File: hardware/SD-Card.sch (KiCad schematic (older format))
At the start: 14 parts

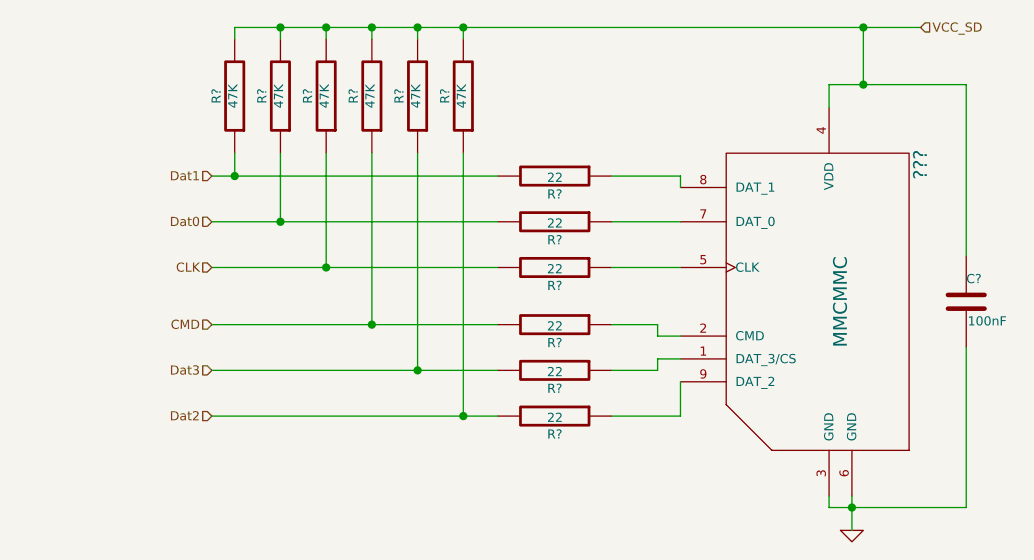
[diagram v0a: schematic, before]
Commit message: Arreglada la distribucion de pines
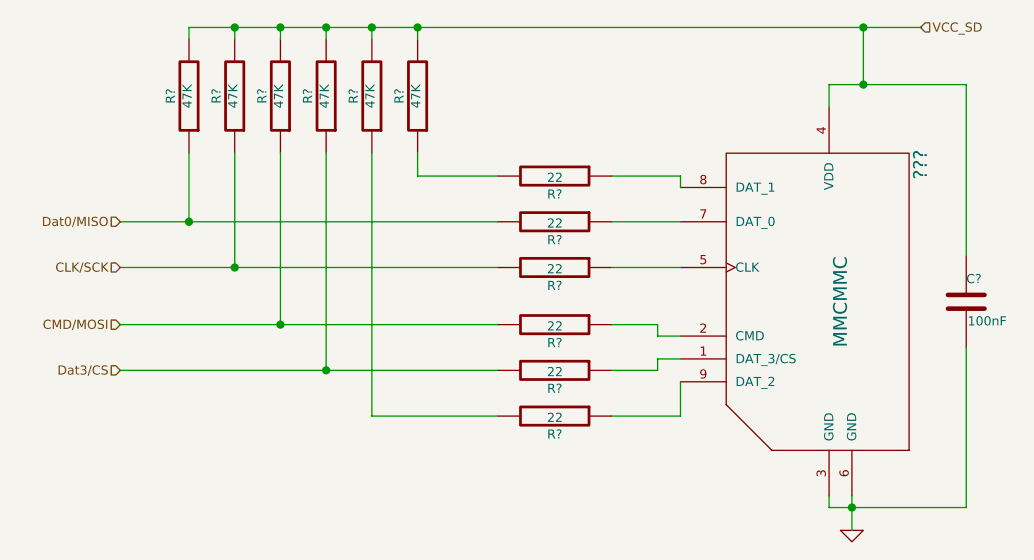
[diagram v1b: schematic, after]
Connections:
- net CLK renamed CLK/SCK
- net CMD renamed CMD/MOSI
- net Dat0 renamed Dat0/MISO
- net Dat1: no longer names the net of R?.1, R?.2
- net Dat2: no longer names the net of R?.1, R?.2
- net Dat3 renamed Dat3/CS
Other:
- moved on the sheet: R?
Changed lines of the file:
@@
 L R R?
 U 1 1 53E03706
-P 4100 2700
-F 0 "R?" V 4180 2700 40  0000 C CNN
-F 1 "47K" V 4107 2701 40  0000 C CNN
-F 2 "" V 4030 2700 30  0000 C CNN
-F 3 "" H 4100 2700 30  0000 C CNN
-	1    4100 2700
+P 3700 2700
+F 0 "R?" V 3780 2700 40  0000 C CNN
+F 1 "47K" V 3707 2701 40  0000 C CNN
+F 2 "" V 3630 2700 30  0000 C CNN
+F 3 "" H 3700 2700 30  0000 C CNN
+	1    3700 2700
 	-1   0    0    1
 $EndComp
@@
 L R R?
 U 1 1 53E03953
+P 3500 2700
+F 0 "R?" V 3580 2700 40  0000 C CNN
+F 1 "47K" V 3507 2701 40  0000 C CNN
+F 2 "" V 3430 2700 30  0000 C CNN
+F 3 "" H 3500 2700 30  0000 C CNN
+	1    3500 2700
+	-1   0    0    1
+$EndComp
+$Comp
+L R R?
+U 1 1 53E0395E
+P 3300 2700
+F 0 "R?" V 3380 2700 40  0000 C CNN
+F 1 "47K" V 3307 2701 40  0000 C CNN
+F 2 "" V 3230 2700 30  0000 C CNN
+F 3 "" H 3300 2700 30  0000 C CNN
+	1    3300 2700
+	-1   0    0    1
+$EndComp
+$Comp
+L R R?
+U 1 1 53E03969
+P 3100 2700
+F 0 "R?" V 3180 2700 40  0000 C CNN
+F 1 "47K" V 3107 2701 40  0000 C CNN
+F 2 "" V 3030 2700 30  0000 C CNN
+F 3 "" H 3100 2700 30  0000 C CNN
+	1    3100 2700
+	-1   0    0    1
+$EndComp
+$Comp
+L R R?
+U 1 1 53E03974
+P 2900 2700
+F 0 "R?" V 2980 2700 40  0000 C CNN
+F 1 "47K" V 2907 2701 40  0000 C CNN
+F 2 "" V 2830 2700 30  0000 C CNN
+F 3 "" H 2900 2700 30  0000 C CNN
+	1    2900 2700
+	-1   0    0    1
+$EndComp
+$Comp
+L R R?
+U 1 1 53E0397F
 P 3900 2700
 F 0 "R?" V 3980 2700 40  0000 C CNN
@@
 	-1   0    0    1
 $EndComp
-$Comp
-L R R?
-U 1 1 53E0395E
-P 3700 2700
-F 0 "R?" V 3780 2700 40  0000 C CNN
-F 1 "47K" V 3707 2701 40  0000 C CNN
-F 2 "" V 3630 2700 30  0000 C CNN
-F 3 "" H 3700 2700 30  0000 C CNN
-	1    3700 2700
-	-1   0    0    1
-$EndComp
-$Comp
-L R R?
-U 1 1 53E03969
-P 3500 2700
-F 0 "R?" V 3580 2700 40  0000 C CNN
-F 1 "47K" V 3507 2701 40  0000 C CNN
-F 2 "" V 3430 2700 30  0000 C CNN
-F 3 "" H 3500 2700 30  0000 C CNN
-	1    3500 2700
-	-1   0    0    1
-$EndComp
-$Comp
-L R R?
-U 1 1 53E03974
-P 3300 2700
-F 0 "R?" V 3380 2700 40  0000 C CNN
-F 1 "47K" V 3307 2701 40  0000 C CNN
-F 2 "" V 3230 2700 30  0000 C CNN
-F 3 "" H 3300 2700 30  0000 C CNN
-	1    3300 2700
-	-1   0    0    1
-$EndComp
-$Comp
-L R R?
-U 1 1 53E0397F
-P 3100 2700
-F 0 "R?" V 3180 2700 40  0000 C CNN
-F 1 "47K" V 3107 2701 40  0000 C CNN
-F 2 "" V 3030 2700 30  0000 C CNN
-F 3 "" H 3100 2700 30  0000 C CNN
-	1    3100 2700
-	-1   0    0    1
-$EndComp
-Text HLabel 3000 3050 0    40   Input ~ 0
-Dat1
-Text HLabel 3000 3250 0    40   Input ~ 0
-Dat0
-Text HLabel 3000 3450 0    40   Input ~ 0
-CLK
-Text HLabel 3000 3700 0    40   Input ~ 0
-CMD
-Text HLabel 3000 3900 0    40   Input ~ 0
-Dat3
-Text HLabel 3000 4100 0    40   Input ~ 0
-Dat2
+Text HLabel 2600 3250 0    40   Input ~ 0
+Dat0/MISO
+Text HLabel 2600 3450 0    40   Input ~ 0
+CLK/SCK
+Text HLabel 2600 3700 0    40   Input ~ 0
+CMD/MOSI
+Text HLabel 2600 3900 0    40   Input ~ 0
+Dat3/CS
 Text HLabel 6100 2400 2    40   Input ~ 0
 VCC_SD
 Wire Wire Line
-	3000 3050 4250 3050
-Wire Wire Line
-	3000 3250 4250 3250
-Wire Wire Line
-	3000 3450 4250 3450
-Wire Wire Line
-	3000 3700 4250 3700
-Wire Wire Line
-	3000 3900 4250 3900
-Wire Wire Line
-	3000 4100 4250 4100
-Wire Wire Line
-	4100 2950 4100 4100
-Connection ~ 4100 4100
-Wire Wire Line
-	3900 2950 3900 3900
-Connection ~ 3900 3900
-Wire Wire Line
-	3700 2950 3700 3700
-Connection ~ 3700 3700
-Wire Wire Line
-	3500 2950 3500 3450
-Connection ~ 3500 3450
-Wire Wire Line
-	3300 2950 3300 3250
-Connection ~ 3300 3250
-Wire Wire Line
-	3100 2950 3100 3050
-Connection ~ 3100 3050
+	2600 3250 4250 3250
+Wire Wire Line
+	2600 3450 4250 3450
+Wire Wire Line
+	2600 3700 4250 3700
+Wire Wire Line
+	2600 3900 4250 3900
+Wire Wire Line
+	3700 2950 3700 4100
+Wire Wire Line
+	3500 2950 3500 3900
+Connection ~ 3500 3900
+Wire Wire Line
+	3300 2950 3300 3700
+Connection ~ 3300 3700
+Wire Wire Line
+	3100 2950 3100 3450
+Connection ~ 3100 3450
+Wire Wire Line
+	2900 2950 2900 3250
+Connection ~ 2900 3250
+Wire Wire Line
+	3900 2950 3900 3050
 $Comp
 L C C?
@@
 Connection ~ 5800 4500
 Wire Wire Line
-	3100 2400 6100 2400
-Wire Wire Line
 	5850 2400 5850 2650
 Connection ~ 5850 2650
 Wire Wire Line
+	3700 2400 3700 2450
+Wire Wire Line
+	3500 2450 3500 2400
+Connection ~ 3500 2400
+Wire Wire Line
+	3300 2450 3300 2400
+Connection ~ 3300 2400
+Wire Wire Line
 	3100 2450 3100 2400
-Wire Wire Line
-	4100 2400 4100 2450
+Connection ~ 3100 2400
+Wire Wire Line
+	2900 2450 2900 2400
+Connection ~ 3700 2400
+Connection ~ 5850 2400
+Wire Wire Line
+	3900 3050 4250 3050
 Wire Wire Line
 	3900 2450 3900 2400
 Connection ~ 3900 2400
 Wire Wire Line
-	3700 2450 3700 2400
-Connection ~ 3700 2400
-Wire Wire Line
-	3500 2450 3500 2400
-Connection ~ 3500 2400
-Wire Wire Line
-	3300 2450 3300 2400
-Connection ~ 3300 2400
-Connection ~ 4100 2400
-Connection ~ 5850 2400
+	3700 4100 4250 4100
+Wire Wire Line
+	2900 2400 6100 2400
 $EndSCHEMATC

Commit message: Terminado el esquematico, iniciado el PCB
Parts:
- C17: renamed from C?; footprint (none) -> Capacitors_SMD:c_1206
- R50, R51, R52, R53, R54, R55, R56, R57, R58, R59, R60, R61: renamed from R?; footprint (none) -> Resistors_SMD:Resistor_SMD1206_ReflowWave
- S1: renamed from ???; value MMCMMC -> SD
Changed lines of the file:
@@
 $EndDescr
 $Comp
-L R R?
+L R R54
 U 1 1 53E03706
 P 3700 2700
-F 0 "R?" V 3780 2700 40  0000 C CNN
+F 0 "R54" V 3780 2700 40  0000 C CNN
 F 1 "47K" V 3707 2701 40  0000 C CNN
-F 2 "" V 3630 2700 30  0000 C CNN
+F 2 "Resistors_SMD:Resistor_SMD1206_ReflowWave" V 3630 2700 30  0001 C CNN
 F 3 "" H 3700 2700 30  0000 C CNN
 	1    3700 2700
@@
 $EndComp
 $Comp
-L R R?
+L R R56
 U 1 1 53E03718
 P 4500 3050
-F 0 "R?" V 4580 3050 40  0000 C CNN
+F 0 "R56" V 4580 3050 40  0000 C CNN
 F 1 "22" V 4507 3051 40  0000 C CNN
-F 2 "" V 4430 3050 30  0000 C CNN
+F 2 "Resistors_SMD:Resistor_SMD1206_ReflowWave" V 4430 3050 30  0001 C CNN
 F 3 "" H 4500 3050 30  0000 C CNN
 	1    4500 3050
@@
 $EndComp
 $Comp
-L R R?
+L R R57
 U 1 1 53E03723
 P 4500 3250
-F 0 "R?" V 4580 3250 40  0000 C CNN
+F 0 "R57" V 4580 3250 40  0000 C CNN
 F 1 "22" V 4507 3251 40  0000 C CNN
-F 2 "" V 4430 3250 30  0000 C CNN
+F 2 "Resistors_SMD:Resistor_SMD1206_ReflowWave" V 4430 3250 30  0001 C CNN
 F 3 "" H 4500 3250 30  0000 C CNN
 	1    4500 3250
@@
 $EndComp
 $Comp
-L R R?
+L R R58
 U 1 1 53E03729
 P 4500 3450
-F 0 "R?" V 4580 3450 40  0000 C CNN
+F 0 "R58" V 4580 3450 40  0000 C CNN
 F 1 "22" V 4507 3451 40  0000 C CNN
-F 2 "" V 4430 3450 30  0000 C CNN
+F 2 "Resistors_SMD:Resistor_SMD1206_ReflowWave" V 4430 3450 30  0001 C CNN
 F 3 "" H 4500 3450 30  0000 C CNN
 	1    4500 3450
@@
 $EndComp
 $Comp
-L R R?
+L R R59
 U 1 1 53E0372F
 P 4500 3700
-F 0 "R?" V 4580 3700 40  0000 C CNN
+F 0 "R59" V 4580 3700 40  0000 C CNN
 F 1 "22" V 4507 3701 40  0000 C CNN
-F 2 "" V 4430 3700 30  0000 C CNN
+F 2 "Resistors_SMD:Resistor_SMD1206_ReflowWave" V 4430 3700 30  0001 C CNN
 F 3 "" H 4500 3700 30  0000 C CNN
 	1    4500 3700
@@
 $EndComp
 $Comp
-L R R?
+L R R60
 U 1 1 53E03735
 P 4500 3900
-F 0 "R?" V 4580 3900 40  0000 C CNN
+F 0 "R60" V 4580 3900 40  0000 C CNN
 F 1 "22" V 4507 3901 40  0000 C CNN
-F 2 "" V 4430 3900 30  0000 C CNN
+F 2 "Resistors_SMD:Resistor_SMD1206_ReflowWave" V 4430 3900 30  0001 C CNN
 F 3 "" H 4500 3900 30  0000 C CNN
 	1    4500 3900
@@
 $EndComp
 $Comp
-L R R?
+L R R61
 U 1 1 53E0373B
 P 4500 4100
-F 0 "R?" V 4580 4100 40  0000 C CNN
+F 0 "R61" V 4580 4100 40  0000 C CNN
 F 1 "22" V 4507 4101 40  0000 C CNN
-F 2 "" V 4430 4100 30  0000 C CNN
+F 2 "Resistors_SMD:Resistor_SMD1206_ReflowWave" V 4430 4100 30  0001 C CNN
 F 3 "" H 4500 4100 30  0000 C CNN
 	1    4500 4100
@@
 	5050 3250 4750 3250
 $Comp
-L MMCMMC ???
+L MMCMMC S1
 U 1 1 53E038EC
 P 5550 3600
-F 0 "???" V 6100 4200 60  0000 C CNN
-F 1 "MMCMMC" V 5750 3600 60  0000 C CNN
-F 2 "" V 5250 3650 60  0000 C CNN
+F 0 "S1" V 6100 4200 60  0000 C CNN
+F 1 "SD" V 5750 3600 60  0000 C CNN
+F 2 "" V 5250 3650 60  0001 C CNN
 F 3 "" V 5250 3650 60  0000 C CNN
 	1    5550 3600
@@
 	5050 3050 4750 3050
 $Comp
-L GND #PWR?
+L GND #PWR054
 U 1 1 53E03916
 P 5800 4600
-F 0 "#PWR?" H 5800 4600 30  0001 C CNN
+F 0 "#PWR054" H 5800 4600 30  0001 C CNN
 F 1 "GND" H 5800 4530 30  0001 C CNN
 F 2 "" H 5800 4600 60  0000 C CNN
@@
 	5800 4450 5800 4600
 $Comp
-L R R?
+L R R53
 U 1 1 53E03953
 P 3500 2700
-F 0 "R?" V 3580 2700 40  0000 C CNN
+F 0 "R53" V 3580 2700 40  0000 C CNN
 F 1 "47K" V 3507 2701 40  0000 C CNN
-F 2 "" V 3430 2700 30  0000 C CNN
+F 2 "Resistors_SMD:Resistor_SMD1206_ReflowWave" V 3430 2700 30  0001 C CNN
 F 3 "" H 3500 2700 30  0000 C CNN
 	1    3500 2700
@@
 $EndComp
 $Comp
-L R R?
+L R R52
 U 1 1 53E0395E
 P 3300 2700
-F 0 "R?" V 3380 2700 40  0000 C CNN
+F 0 "R52" V 3380 2700 40  0000 C CNN
 F 1 "47K" V 3307 2701 40  0000 C CNN
-F 2 "" V 3230 2700 30  0000 C CNN
+F 2 "Resistors_SMD:Resistor_SMD1206_ReflowWave" V 3230 2700 30  0001 C CNN
 F 3 "" H 3300 2700 30  0000 C CNN
 	1    3300 2700
@@
 $EndComp
 $Comp
-L R R?
+L R R51
 U 1 1 53E03969
 P 3100 2700
-F 0 "R?" V 3180 2700 40  0000 C CNN
+F 0 "R51" V 3180 2700 40  0000 C CNN
 F 1 "47K" V 3107 2701 40  0000 C CNN
-F 2 "" V 3030 2700 30  0000 C CNN
+F 2 "Resistors_SMD:Resistor_SMD1206_ReflowWave" V 3030 2700 30  0001 C CNN
 F 3 "" H 3100 2700 30  0000 C CNN
 	1    3100 2700
@@
 $EndComp
 $Comp
-L R R?
+L R R50
 U 1 1 53E03974
 P 2900 2700
-F 0 "R?" V 2980 2700 40  0000 C CNN
+F 0 "R50" V 2980 2700 40  0000 C CNN
 F 1 "47K" V 2907 2701 40  0000 C CNN
-F 2 "" V 2830 2700 30  0000 C CNN
+F 2 "Resistors_SMD:Resistor_SMD1206_ReflowWave" V 2830 2700 30  0001 C CNN
 F 3 "" H 2900 2700 30  0000 C CNN
 	1    2900 2700
@@
 $EndComp
 $Comp
-L R R?
+L R R55
 U 1 1 53E0397F
 P 3900 2700
-F 0 "R?" V 3980 2700 40  0000 C CNN
+F 0 "R55" V 3980 2700 40  0000 C CNN
 F 1 "47K" V 3907 2701 40  0000 C CNN
-F 2 "" V 3830 2700 30  0000 C CNN
+F 2 "Resistors_SMD:Resistor_SMD1206_ReflowWave" V 3830 2700 30  0001 C CNN
 F 3 "" H 3900 2700 30  0000 C CNN
 	1    3900 2700
@@
 	3900 2950 3900 3050
 $Comp
-L C C?
+L C C17
 U 1 1 53E03B3A
 P 6300 3600
-F 0 "C?" H 6300 3700 40  0000 L CNN
+F 0 "C17" H 6300 3700 40  0000 L CNN
 F 1 "100nF" H 6306 3515 40  0000 L CNN
-F 2 "" H 6338 3450 30  0000 C CNN
+F 2 "Capacitors_SMD:c_1206" H 6338 3450 30  0001 C CNN
 F 3 "" H 6300 3600 60  0000 C CNN
 	1    6300 3600

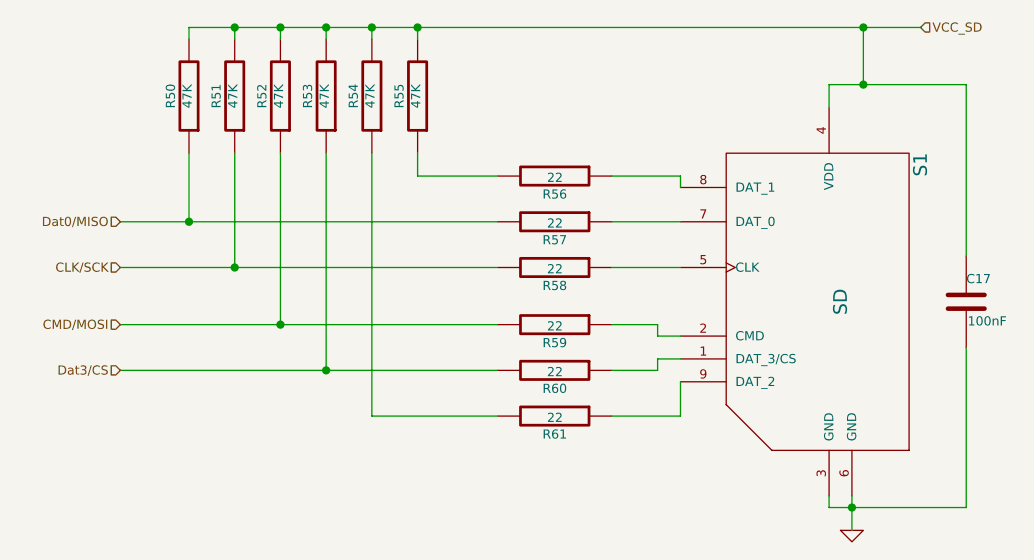
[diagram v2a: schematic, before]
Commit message: Terminado el Routeo de la Placa
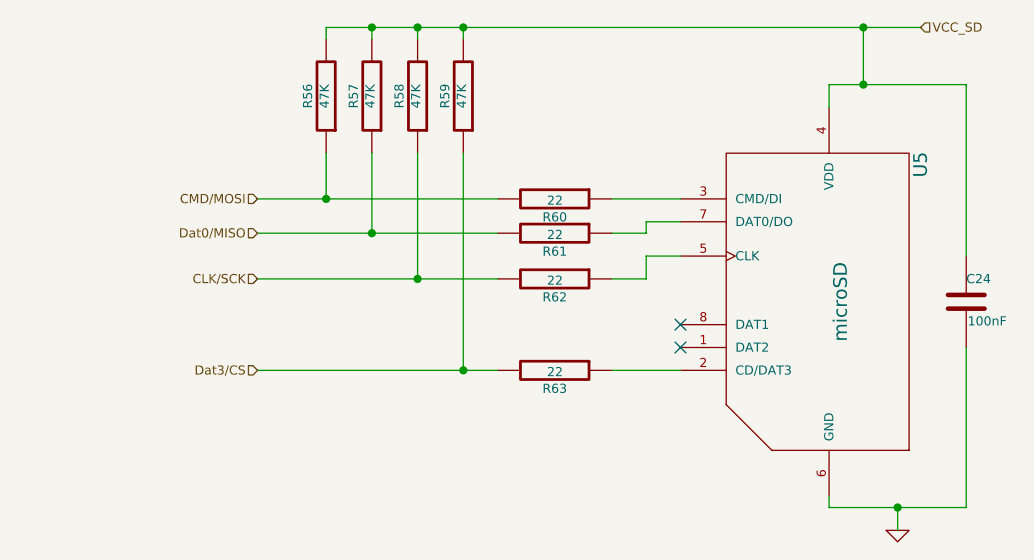
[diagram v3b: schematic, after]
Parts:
- removed R54, R55: 47K, Resistors_SMD:Resistor_SMD1206_ReflowWave, symbol R
- removed R56, R61: 22, Resistors_SMD:Resistor_SMD1206_ReflowWave, symbol R
- removed S1: SD, symbol MMCMMC
- added U5: microSD, w_Connectors:microSD, symbol microSD
- C24: renamed from C17; footprint Capacitors_SMD:c_1206 -> Capacitors_SMD:c_0805
- R56: renamed from R50; footprint Resistors_SMD:Resistor_SMD1206_ReflowWave -> Resistors_SMD:R_0805
- R57: renamed from R51; footprint Resistors_SMD:Resistor_SMD1206_ReflowWave -> Resistors_SMD:R_0805
- R58: renamed from R52; footprint Resistors_SMD:Resistor_SMD1206_ReflowWave -> Resistors_SMD:R_0805
- R59: renamed from R53; footprint Resistors_SMD:Resistor_SMD1206_ReflowWave -> Resistors_SMD:R_0805
- R60: renamed from R57; footprint Resistors_SMD:Resistor_SMD1206_ReflowWave -> Resistors_SMD:R_0805
- R61: renamed from R58; footprint Resistors_SMD:Resistor_SMD1206_ReflowWave -> Resistors_SMD:R_0805
- R62: renamed from R59; footprint Resistors_SMD:Resistor_SMD1206_ReflowWave -> Resistors_SMD:R_0805
- R63: renamed from R60; footprint Resistors_SMD:Resistor_SMD1206_ReflowWave -> Resistors_SMD:R_0805
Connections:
- net CLK/SCK: now also R58.1, R62.2; no longer R57.1, R61.2
- net CMD/MOSI: now also R56.1, R60.2; no longer R58.1, R62.2
- net Dat0/MISO: now also R57.1, R61.2; no longer R56.1, R60.2
- net GND: now also U5.6 (GND)
- net VCC_SD: now also U5.4 (VDD)
- net at R60.1: now also U5.3 (CMD/DI)
- net at R61.1: now also U5.7 (DAT0/DO)
- net at R62.1: now also U5.5 (CLK)
- net at R63.1: now also U5.2 (CD/DAT3)
- no-connect marks 0 -> 2
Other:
- moved on the sheet: R56, R57, R58, R59, R60, R61, R62

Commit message: Placa terminada, serigrafia verificada, logos agregados
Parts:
- C24: footprint Capacitors_SMD:c_0805 -> w_Connectors:c_0805
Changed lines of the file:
@@
 F 0 "C24" H 6300 3700 40  0000 L CNN
 F 1 "100nF" H 6306 3515 40  0000 L CNN
-F 2 "Capacitors_SMD:c_0805" H 6338 3450 30  0001 C CNN
+F 2 "w_Connectors:c_0805" H 6338 3450 30  0001 C CNN
 F 3 "" H 6300 3600 60  0000 C CNN
 	1    6300 3600
